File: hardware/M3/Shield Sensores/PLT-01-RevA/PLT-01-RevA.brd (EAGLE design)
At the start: 68.6 x 53.6 mm, 5 parts

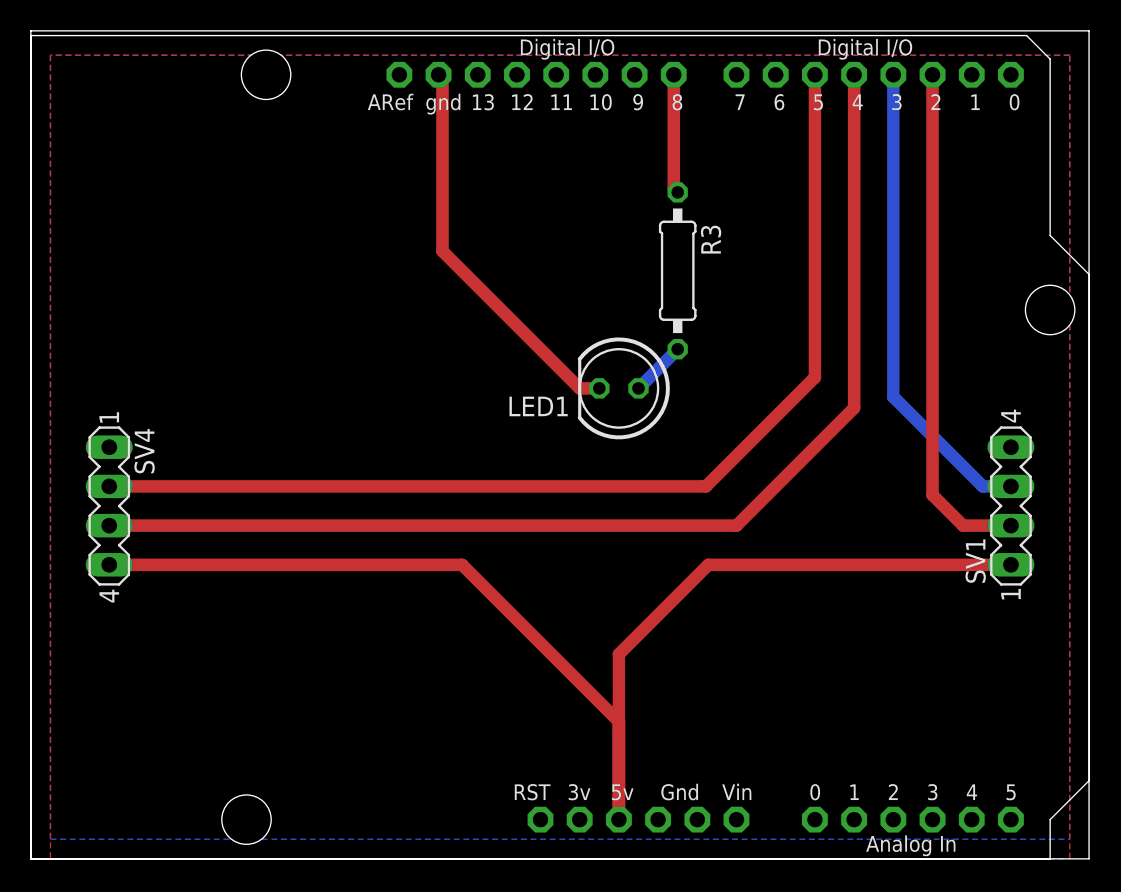
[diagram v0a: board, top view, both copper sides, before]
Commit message: Archivos a png
paso archivos de cnc a png para que se puedan ver los cortes sin tener que descargar aplicaciones
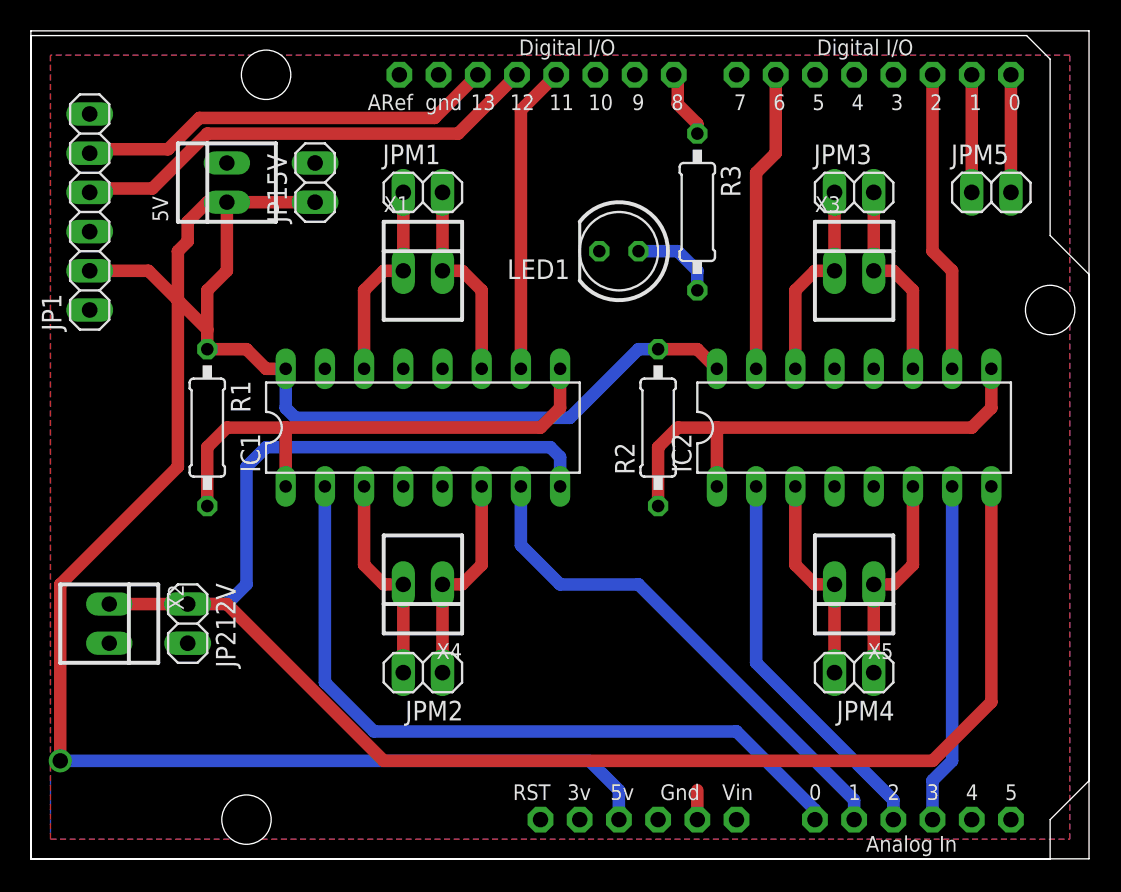
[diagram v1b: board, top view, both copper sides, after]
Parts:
- removed SV1, SV4: (no value), con-lstb:MA04-1
- added 5V, X1, X2, X3, X4, X5: 22-23-2021, con-molex:22-23-2021
- added IC1, IC2: L293D, st-microelectronics:DIL16
- added JP1: (no value), pinhead:1X06
- added JP15V, JP212V, JPM1, JPM2, JPM3, JPM4, JPM5: (no value), pinhead:1X02
- added R1, R2: (no value), resistor:0207/10
- moved LED1 8.89 mm to (47.0, 43.2)
- moved R3 4.02 mm to (52.1, 45.7)
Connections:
- removed net GND1: U$1.GND1
- removed net GND2: U$1.GND2
- removed net P2A: SV1.2, U$1.D2
- removed net P3A: SV1.3, U$1.D3
- removed net P4A: SV4.3, U$1.D4
- removed net P5A: SV4.2, U$1.D5
- removed net P6A: U$1.D6
- removed net P7A: U$1.D7
- new net 1A1: IC1.2, U$1.A0
- new net 1A2: IC2.2, U$1.A2
- new net 2A1: IC1.7, U$1.A1
- new net 2A2: IC2.7, U$1.A3
- new net 3A2: IC2.10, U$1.D2
- new net 4A2: IC2.15, U$1.D6
- new net N$1: IC1.3, JPM2.2, X4.2
- new net N$11: IC1.10, U$1.D11
- new net N$13: JP1.4, U$1.D12
- new net N$14: IC1.1, IC1.9, R1.2
- new net N$19: JP1.5, U$1.D13
- new net N$2: IC1.6, JPM2.1, X4.1
- new net N$22: IC1.15, U$1.D10
- new net N$3: IC2.3, JPM4.2, X5.2
- new net N$4: IC2.6, JPM4.1, X5.1
- new net N$5: IC2.14, JPM3.1, X3.1
- new net N$6: IC2.11, JPM3.2, X3.2
- new net N$7: IC1.14, JPM1.1, X1.1
- new net N$8: IC1.11, JPM1.2, X1.2
- new net N$9: IC2.1, IC2.9, R2.1
- new net RX: JPM5.2, U$1.D0
- new net TX: JPM5.1, U$1.D1
- new net VCC2: IC1.8, IC2.8, JP212V.1, X2.1
- net 5V: now also 5V.1, IC1.16, IC2.16, JP1.2, JP15V.1, R1.1, R2.2; no longer SV1.1, SV4.4
- net GND: now also 5V.2, IC1.12, IC1.13, IC1.4, IC1.5, IC2.12, IC2.13, IC2.4, IC2.5, JP1.3, JP15V.2, JP212V.2, U$1.GND1, U$1.GND2, X2.2; no longer SV1.4, SV4.1
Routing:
- net VCC2: track 0.00 -> 111.9 mm
- net P4A: track 73.0 -> 0.00 mm
- net P5A: track 68.3 -> 0.00 mm
- net 5V: track 82.1 -> 145.2 mm, vias 0 -> 1
- net 1A1: track 0.00 -> 48.5 mm
- net N$14: track 0.00 -> 34.1 mm
- net 2A1: track 0.00 -> 33.5 mm
- net P2A: track 33.1 -> 0.00 mm
- net N$9: track 0.00 -> 32.8 mm
- net N$13: track 0.00 -> 31.0 mm
- net P3A: track 30.9 -> 0.00 mm
- net N$19: track 0.00 -> 27.4 mm
- net 1A2: track 0.00 -> 25.3 mm
- net GND: track 25.3 -> 1.91 mm
- net 2A2: track 0.00 -> 22.1 mm
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
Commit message: Actualizaciones
cambios en placa 2
cambio de ubicacion de la carpeta vehiculo
agregamos archivos svg y redimensionados
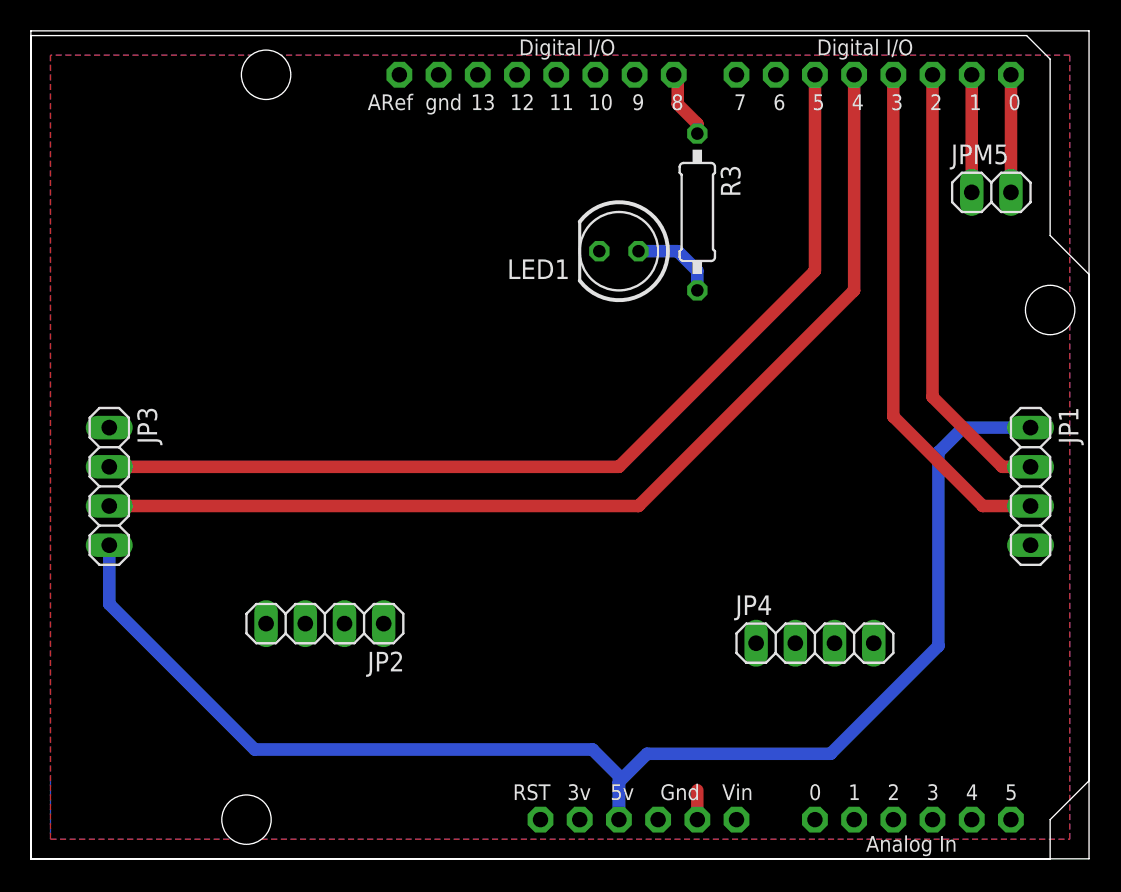
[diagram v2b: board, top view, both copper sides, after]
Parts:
- removed 5V, X1, X2, X3, X4, X5: 22-23-2021, con-molex:22-23-2021
- removed IC1, IC2: L293D, st-microelectronics:DIL16
- removed JP15V, JP212V, JPM1, JPM2, JPM3, JPM4: (no value), pinhead:1X02
- removed R1, R2: (no value), resistor:0207/10
- added JP2, JP3, JP4: (no value), pinhead:1X04
- JP1: device pinhead:1X06 -> pinhead:1X04
- moved JP1 63.5 mm to (73.7, 27.9), turned to 270 degrees
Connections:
- removed net 1A1: IC1.2, U$1.A0
- removed net 1A2: IC2.2, U$1.A2
- removed net 2A1: IC1.7, U$1.A1
- removed net 2A2: IC2.7, U$1.A3
- removed net 3A2: IC2.10, U$1.D2
- removed net 4A2: IC2.15, U$1.D6
- removed net N$1: IC1.3, JPM2.2, X4.2
- removed net N$11: IC1.10, U$1.D11
- removed net N$13: JP1.4, U$1.D12
- removed net N$2: IC1.6, JPM2.1, X4.1
- removed net N$22: IC1.15, U$1.D10
- removed net N$3: IC2.3, JPM4.2, X5.2
- removed net N$6: IC2.11, JPM3.2, X3.2
- removed net N$7: IC1.14, JPM1.1, X1.1
- removed net VCC2: IC1.8, IC2.8, JP212V.1, X2.1
- new net N$15: JP2.1
- new net N$17: JP4.2
- new net N$30: U$1.D7
- new net N$31: U$1.D10
- new net N$32: U$1.D12
- new net N$35: U$1.D6
- new net N$36: U$1.D9
- new net N$37: U$1.D11
- new net P2A: JP1.2, U$1.D2
- new net P3A: JP1.3, U$1.D3
- new net P4A: JP3.3, U$1.D4
- new net P5A: JP3.2, U$1.D5
- net 5V: now also JP1.1, JP3.4; no longer 5V.1, IC1.16, IC2.16, JP1.2, JP15V.1, R1.1, R2.2
- net GND: now also JP1.4, JP3.1; no longer 5V.2, IC1.12, IC1.13, IC1.4, IC1.5, IC2.12, IC2.13, IC2.4, IC2.5, JP1.3, JP15V.2, JP212V.2, X2.2
- net N$14: now also JP2.3; no longer IC1.1, IC1.9, R1.2
- net N$19: now also JP4.4; no longer JP1.5, U$1.D13
- net N$4: now also JP2.4; no longer IC2.6, JPM4.1, X5.1
- net N$5: now also JP2.2; no longer IC2.14, JPM3.1, X3.1
- net N$8: now also JP4.1; no longer IC1.11, JPM1.2, X1.2
- net N$9: now also JP4.3; no longer IC2.1, IC2.9, R2.1
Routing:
- net VCC2: track 111.9 -> 0.00 mm
- net P4A: track 0.00 -> 68.7 mm
- net P5A: track 0.00 -> 63.7 mm
- net 5V: track 145.2 -> 90.2 mm, vias 1 -> 0
- net 1A1: track 48.5 -> 0.00 mm
- net N$14: track 34.1 -> 0.00 mm
- net 2A1: track 33.5 -> 0.00 mm
- net P3A: track 0.00 -> 33.4 mm
- net N$9: track 32.8 -> 0.00 mm
- net N$13: track 31.0 -> 0.00 mm
- net P2A: track 0.00 -> 29.1 mm
- net N$19: track 27.4 -> 0.00 mm
- net 1A2: track 25.3 -> 0.00 mm
- net 2A2: track 22.1 -> 0.00 mm
- net N$11: track 20.0 -> 0.00 mm
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
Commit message: pequeño cambio en shield sensores
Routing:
- net GND: track 1.91 -> 78.5 mm
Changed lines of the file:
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@@
 <contactref element="JP1" pad="4"/>
 <contactref element="JP3" pad="1"/>
+<wire x1="13.97" y1="31.75" x2="35.306" y2="53.086" width="0.8128" layer="1"/>
+<wire x1="35.306" y1="53.086" x2="35.306" y2="54.61" width="0.8128" layer="1"/>
+<wire x1="53.7788375" y1="8.3566" x2="52.6034" y2="7.1811625" width="0.8128" layer="1"/>
+<wire x1="73.66" y1="24.13" x2="57.8866" y2="8.3566" width="0.8128" layer="1"/>
+<wire x1="52.6034" y1="7.1811625" x2="52.6034" y2="6.8834" width="0.8128" layer="1"/>
+<wire x1="52.6034" y1="6.8834" x2="52.07" y2="6.35" width="0.8128" layer="1"/>
+<wire x1="57.8866" y1="8.3566" x2="53.7788375" y2="8.3566" width="0.8128" layer="1"/>
+<wire x1="45.72" y1="43.18" x2="35.306" y2="53.594" width="0.8128" layer="1"/>
+<wire x1="35.306" y1="53.594" x2="35.306" y2="54.61" width="0.8128" layer="1"/>
+<wire x1="49.53" y1="6.35" x2="52.07" y2="6.35" width="0" layer="19" extent="1-1"/>
+<wire x1="45.72" y1="43.18" x2="73.66" y2="24.13" width="0" layer="19" extent="1-1"/>
 </signal>
 <signal name="VIN">

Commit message: Se corrigen pistas GND
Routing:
- net GND: track 78.5 -> 11.3 mm
- net 5V: track 90.2 -> 87.5 mm
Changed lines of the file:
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@@
 <drawing>
 <settings>
-<setting alwaysvectorfont="no"/>
+<setting alwaysvectorfont="yes"/>
 <setting keepoldvectorfont="yes"/>
 <setting verticaltext="up"/>
@@
 <contactref element="JP1" pad="4"/>
 <contactref element="JP3" pad="1"/>
-<wire x1="13.97" y1="31.75" x2="35.306" y2="53.086" width="0.8128" layer="1"/>
 <wire x1="35.306" y1="53.086" x2="35.306" y2="54.61" width="0.8128" layer="1"/>
 <wire x1="53.7788375" y1="8.3566" x2="52.6034" y2="7.1811625" width="0.8128" layer="1"/>
-<wire x1="73.66" y1="24.13" x2="57.8866" y2="8.3566" width="0.8128" layer="1"/>
 <wire x1="52.6034" y1="7.1811625" x2="52.6034" y2="6.8834" width="0.8128" layer="1"/>
 <wire x1="52.6034" y1="6.8834" x2="52.07" y2="6.35" width="0.8128" layer="1"/>
 <wire x1="57.8866" y1="8.3566" x2="53.7788375" y2="8.3566" width="0.8128" layer="1"/>
-<wire x1="45.72" y1="43.18" x2="35.306" y2="53.594" width="0.8128" layer="1"/>
 <wire x1="35.306" y1="53.594" x2="35.306" y2="54.61" width="0.8128" layer="1"/>
-<wire x1="49.53" y1="6.35" x2="52.07" y2="6.35" width="0" layer="19" extent="1-1"/>
-<wire x1="45.72" y1="43.18" x2="73.66" y2="24.13" width="0" layer="19" extent="1-1"/>
 </signal>
 <signal name="VIN">
@@
 <contactref element="JP1" pad="1"/>
 <contactref element="JP3" pad="4"/>
-<wire x1="73.66" y1="31.75" x2="69.29313125" y2="31.75" width="0.8128" layer="16"/>
-<wire x1="69.29313125" y1="31.75" x2="67.691" y2="30.14786875" width="0.8128" layer="16"/>
-<wire x1="48.81456875" y1="10.6172" x2="46.99" y2="8.79263125" width="0.8128" layer="16"/>
-<wire x1="46.99" y1="6.35" x2="46.99" y2="8.79263125" width="0.8128" layer="16"/>
-<wire x1="67.691" y1="30.14786875" x2="67.691" y2="17.60413125" width="0.8128" layer="16"/>
-<wire x1="67.691" y1="17.60413125" x2="60.70406875" y2="10.6172" width="0.8128" layer="16"/>
-<wire x1="60.70406875" y1="10.6172" x2="48.81456875" y2="10.6172" width="0.8128" layer="16"/>
-<wire x1="45.2811625" y1="10.8966" x2="46.99" y2="9.1877625" width="0.8128" layer="16"/>
-<wire x1="46.99" y1="9.1877625" x2="46.99" y2="6.35" width="0.8128" layer="16"/>
-<wire x1="23.3934" y1="10.8966" x2="13.97" y2="20.32" width="0.8128" layer="16"/>
+<wire x1="13.97" y1="20.32" x2="23.3934" y2="10.8966" width="0.8128" layer="16"/>
 <wire x1="13.97" y1="24.13" x2="13.97" y2="20.32" width="0.8128" layer="16"/>
-<wire x1="23.3934" y1="10.8966" x2="45.2811625" y2="10.8966" width="0.8128" layer="16"/>
+<wire x1="23.3934" y1="10.8966" x2="46.99" y2="10.8966" width="0.8128" layer="16"/>
+<wire x1="46.99" y1="10.8966" x2="60.8076" y2="10.8966" width="0.8128" layer="16"/>
+<wire x1="60.8076" y1="10.8966" x2="67.31" y2="17.399" width="0.8128" layer="16"/>
+<wire x1="67.31" y1="17.399" x2="67.31" y2="29.21" width="0.8128" layer="16"/>
+<wire x1="67.31" y1="29.21" x2="69.85" y2="31.75" width="0.8128" layer="16"/>
+<wire x1="69.85" y1="31.75" x2="73.66" y2="31.75" width="0.8128" layer="16"/>
+<wire x1="46.99" y1="6.35" x2="46.99" y2="10.8966" width="0.8128" layer="16"/>
 </signal>
 <signal name="N$30">
